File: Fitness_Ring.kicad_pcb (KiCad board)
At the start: 2 copper layers, 30 parts, among them U1 NRF52832-QFAA-R, U2 MAX30102, U3 MIC5370-SGYMT-TR, U4 MCP73831-2-OT, U5 TXS0102DQE, U6 MAX30205MTA_, Y1 32.768kHz

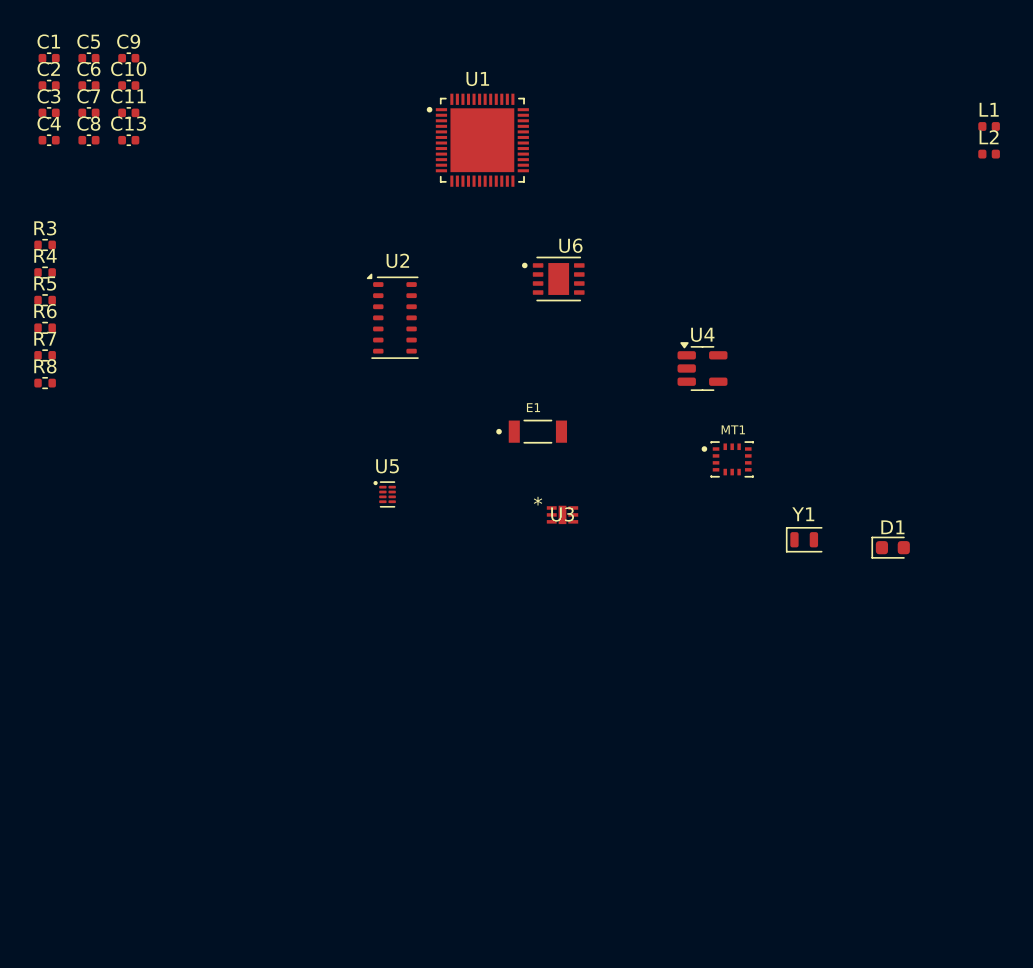
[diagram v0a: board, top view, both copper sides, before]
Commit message: placed all components on the PCB, need to make sure to change schematic so that MAX30102 has its own separate I2C bus
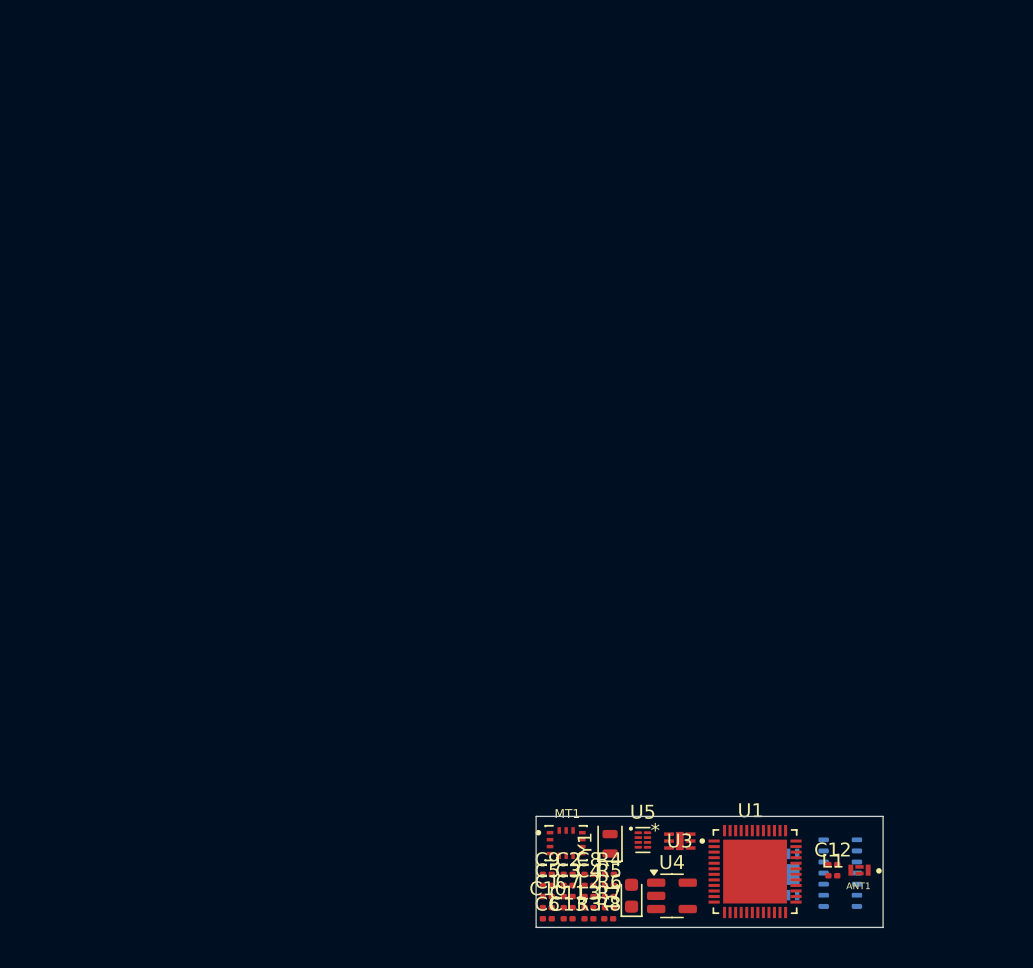
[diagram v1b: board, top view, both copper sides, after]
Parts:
- removed E1: 2450AT18B100E, Fitness:Battery
- added ANT1: ANT016008LCS2442MA2, Fitness:ANT_ANT016008LCS2442MA2, F.Cu at (75.2, 80.1)
- added C12: 1pF, Capacitor_SMD:C_0201_0603Metric, F.Cu at (73.3, 79.7)
- added L3: 3.3nH, Inductor_SMD:L_0201_0603Metric, F.Cu at (55.7, 82.8)
- C1, C10, C11, C13, C2, C3, C4, C5, C6, C7, C8, C9: footprint Capacitor_SMD:C_0402_1005Metric -> Capacitor_SMD:C_0201_0603Metric
- L1, L2: footprint Inductor_SMD:L_0402_1005Metric -> Inductor_SMD:L_0201_0603Metric
- R3, R4, R5, R6, R7, R8: footprint Resistor_SMD:R_0402_1005Metric -> Resistor_SMD:R_0201_0603Metric
- U2, U6: moved to B.Cu
- moved C1 70.3 mm to (52.7, 82.0)
- moved C6 68.5 mm to (52.7, 83.6)
- moved C5 68.1 mm to (52.7, 81.2)
- moved C2 68.0 mm to (54.2, 80.4)
- moved C3 67.1 mm to (54.2, 81.2)
- moved C10 66.5 mm to (52.7, 82.8)
- moved C4 66.3 mm to (55.7, 81.2)
- moved C7 66.2 mm to (54.2, 82.0)
- moved C9 66.1 mm to (52.7, 80.4)
- moved C11 65.4 mm to (54.2, 82.8)
- moved C13 64.4 mm to (54.2, 83.6)
- moved C8 64.0 mm to (55.7, 80.4)
- moved R3 62.4 mm to (55.7, 83.6)
- moved L2 60.8 mm to (55.7, 82.0)
- moved R4 59.4 mm to (57.2, 80.4)
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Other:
- board outline added: 25 x 8 mm

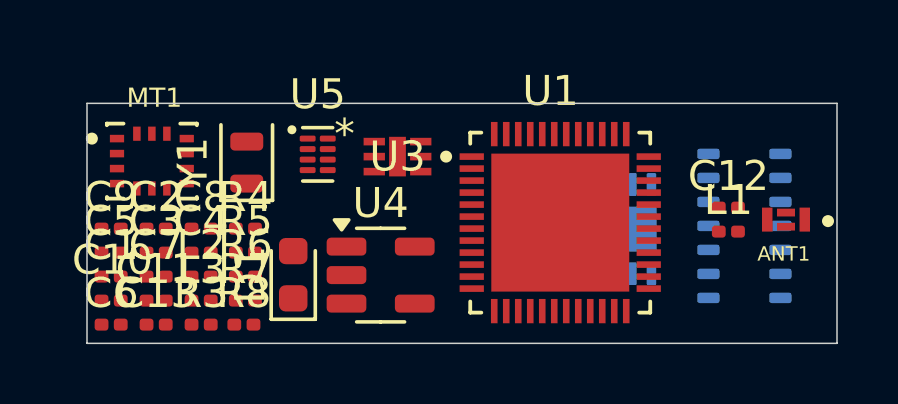
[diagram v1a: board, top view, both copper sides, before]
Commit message: Removed the level translator as we do not need it anymore, switching to a flex PCB with two layers to fix the trace impedance width problem while not going up too much in cost, will work on that next time
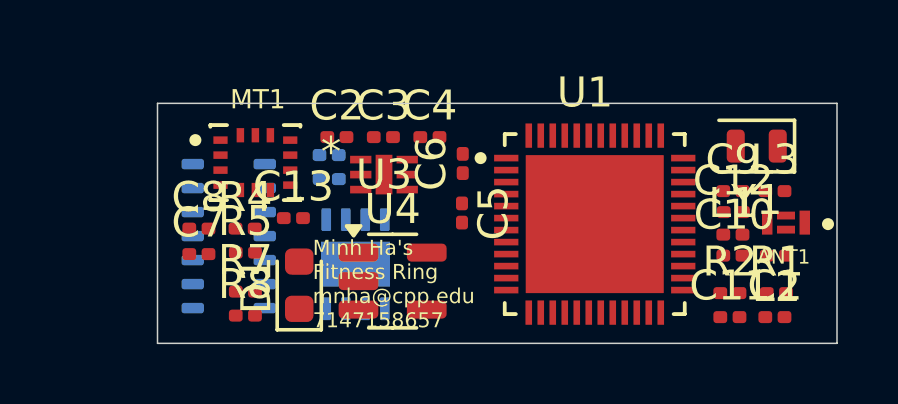
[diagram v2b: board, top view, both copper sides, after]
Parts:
- removed U5: TXS0102DQE, Package_SON:X2SON-8_1.4x1mm_P0.35mm
- added R1: 4.7K, Resistor_SMD:R_0201_0603Metric, F.Cu at (74.9, 82.5)
- added R2: 4.7K, Resistor_SMD:R_0201_0603Metric, F.Cu at (73.3, 82.5)
- R3, R6: moved to B.Cu
- moved C1 22.2 mm to (74.8, 83.3)
- moved C10 20.8 mm to (73.4, 81.3)
- moved C9 20.8 mm to (73.4, 79.2)
- moved L3 19.5 mm to (74.8, 79.2)
- moved L2 19.2 mm to (74.9, 81.3), turned to 180 degrees
- moved C11 19.1 mm to (73.3, 83.3)
- moved U2 17.2 mm to (56.6, 80.7)
- moved Y1 17.0 mm to (74.2, 77.7), turned to 180 degrees
- moved C6 12.9 mm to (64.4, 78.2), turned to 90 degrees
- moved C5 11.8 mm to (64.4, 79.9), turned to -90 degrees
- moved U6 8.97 mm to (60.8, 81.6)
- moved C4 8.54 mm to (63.3, 77.3)
- moved C3 8.50 mm to (61.8, 77.3)
- moved R3 7.08 mm to (59.9, 78.0), turned to 180 degrees
- moved C2 6.75 mm to (60.2, 77.3)
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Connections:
- U1 pad 28: unconnected-(U1-P0_23-Pad28) -> /SCL_MAX
- U1 pad 29: unconnected-(U1-P0_24-Pad29) -> /SDA_MAX
- U2 pad 2: Net-(U2-SCL) -> /SCL_MAX
- U2 pad 3: Net-(U2-SDA) -> /SDA_MAX
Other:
- board size 25 x 8 mm -> 22.6 x 8 mm
- board text added: "Minh Ha's Fitness Ring mnha@cpp.edu 7147158657"

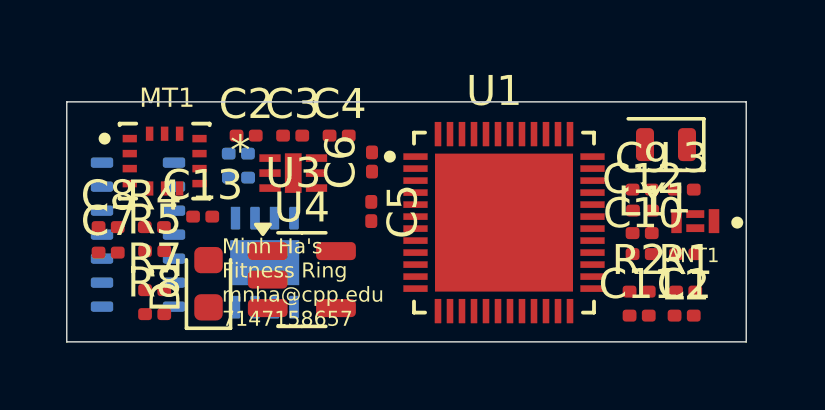
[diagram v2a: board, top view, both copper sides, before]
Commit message: changed the board to a flex board, added keepout zones and ground pour for bottom layer, need to fix Antenna
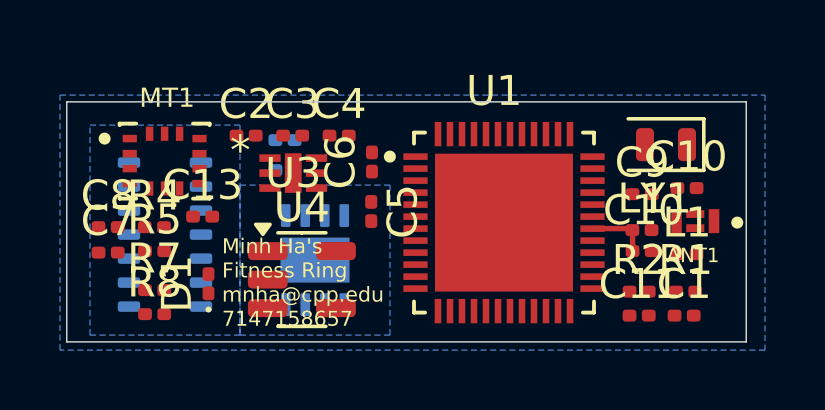
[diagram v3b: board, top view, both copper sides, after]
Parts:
- removed C12: 1pF, Capacitor_SMD:C_0201_0603Metric
- removed L2: 2.7nH, Inductor_SMD:L_0201_0603Metric
- removed L3: 3.3nH, Inductor_SMD:L_0201_0603Metric
- added C10: 1pF, Capacitor_SMD:C_0201_0603Metric, F.Cu at (74.9, 79.1)
- added L1: 3.3nH, Inductor_SMD:L_0201_0603Metric, F.Cu at (74.9, 81.3)
- D1: footprint LED_SMD:LED_0603_1608Metric -> LED_SMD:LED_0201_0603Metric
- moved U6 1.68 mm to (62.5, 81.5)
- moved R3 1.62 mm to (61.5, 77.5)
- moved R6 1.57 mm to (61.5, 78.5)
- moved U2 0.90 mm to (57.5, 80.7)
- moved C9 0.15 mm to (73.4, 79.3)
- moved L1 0.10 mm to (73.4, 80.5)
- moved C10 0.10 mm to (73.4, 81.2)
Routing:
- net Net-(U1-ANT): track 0.00 -> 2.10 mm
- added copper zone on B.Cu, net (none)
- added copper zone on B.Cu, net GND

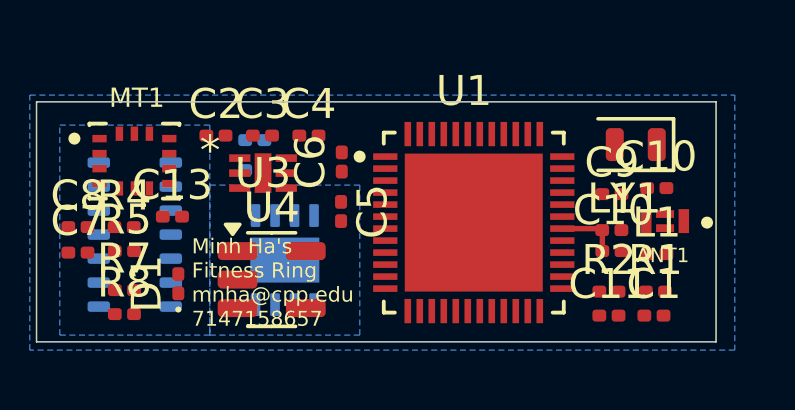
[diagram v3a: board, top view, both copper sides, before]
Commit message: Fixed RF pi network and began doing traces
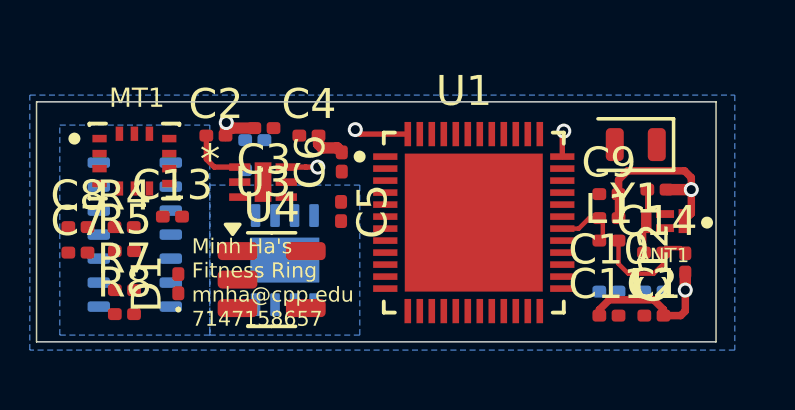
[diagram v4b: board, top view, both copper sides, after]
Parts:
- removed the C10 at (73.4, 81.2)
- removed the C10 at (74.9, 79.1)
- removed the L1 at (73.4, 80.5)
- removed the L1 at (74.9, 81.3)
- added C10: 1pF, Capacitor_SMD:C_0201_0603Metric, F.Cu at (73.3, 80.1)
- added C12: 1pF, Capacitor_SMD:C_0201_0603Metric, F.Cu at (75.8, 81.6)
- added C14: 1pF, Capacitor_SMD:C_0201_0603Metric, F.Cu at (74.9, 79.2)
- added L1: 3.3nH, Inductor_SMD:L_0201_0603Metric, F.Cu at (73.3, 80.8)
- added L2: 1.2nH, Inductor_SMD:L_0201_0603Metric, F.Cu at (74.8, 81.2)
- R1, R2: moved to B.Cu
- moved U3 0.30 mm to (61.8, 78.9)
- moved C3 0.25 mm to (61.8, 77.1), turned to 180 degrees
- moved C9 0.10 mm to (73.3, 79.3)
- turned R1 to 180 degrees
- turned R2 to 180 degrees
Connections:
- ANT1 pad 4: /ANT -> /RF
- U1 pad 30: Net-(U1-ANT) -> /ANT
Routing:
- net GND: track 0.00 -> 13.8 mm, vias 0 -> 3
- net Net-(C12-Pad2): track 0.00 -> 3.82 mm
- net +3.3V: track 0.00 -> 3.73 mm, vias 0 -> 3
- net /RF: track 0.00 -> 2.15 mm
- net Net-(U1-ANT): track 2.10 -> 0.00 mm
- net /ANT: track 0.09 -> 2.19 mm
- net /VBAT: track 0.00 -> 2.01 mm

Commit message: worked on more routing
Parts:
- moved R8 1.04 mm to (57.4, 82.3), turned to 180 degrees
- moved R7 0.61 mm to (57.4, 83.0), turned to 180 degrees
- turned C7 to 180 degrees
- turned C8 to 180 degrees
- turned R4 to 180 degrees
- turned R5 to 180 degrees
- turned Y1 to 0 degrees
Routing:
- net GND: track 13.8 -> 25.9 mm, vias 3 -> 9
- net +3.3V: track 3.73 -> 13.2 mm, vias 3 -> 4
- net Net-(U1-XC2): track 0.00 -> 4.76 mm
- net +5V: track 0.00 -> 3.04 mm, vias 0 -> 3
- net Net-(U1-XC1): track 0.00 -> 2.45 mm
- net Net-(U3-EN1): track 0.00 -> 2.28 mm
- net Net-(U1-DEC1): track 0.00 -> 1.02 mm
- net /INT_IMU_TAP: track 0.00 -> 0.80 mm
- net /SCL_MAX: track 0.00 -> 0.45 mm, vias 0 -> 1
- net (no net): vias 0 -> 1
